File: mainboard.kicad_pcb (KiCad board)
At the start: 2 copper layers, 145.3 x 145.7 mm, 60 parts, among them J1 DRV8833-1, J13 Conn_PCA9685, J14 Conn_01x02, J15 Conn_01x02, J16 Conn_01x02, J18 Screw_Terminal_01x06, J19 Screw_Terminal_01x06, J2 DRV8833-0, J20 Screw_Terminal_01x06, J21 Screw_Terminal_01x06, J22 Screw_Terminal_01x06, J23 Screw_Terminal_01x06, J24 Screw_Terminal_01x04, J25 Screw_Terminal_01x02, J27 Rotary Encoder Conn, J28 Conn_01x02, J3 Conn_01x02, J4 Screw_Terminal_01x06, J5 Screw_Terminal_01x06, J6 VIM4_HEADER, J7 Screw_Terminal_01x06, J8 Screw_Terminal_01x06, Q3 2N7000, Q4 2N7000, U1 MCP23017_SP

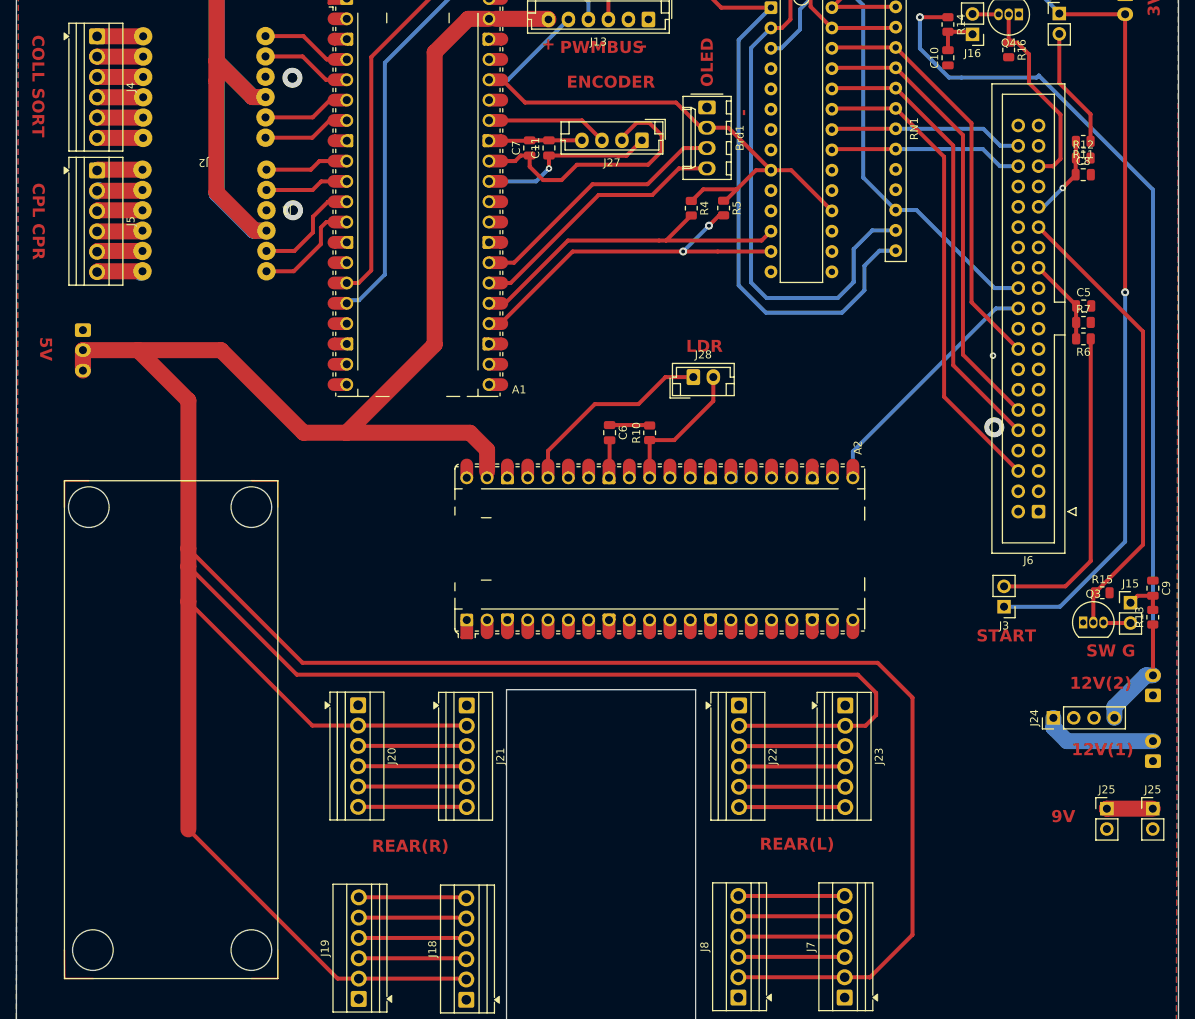
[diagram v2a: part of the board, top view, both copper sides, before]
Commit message: 0 Error DRC mainboard V1.1
Little edits
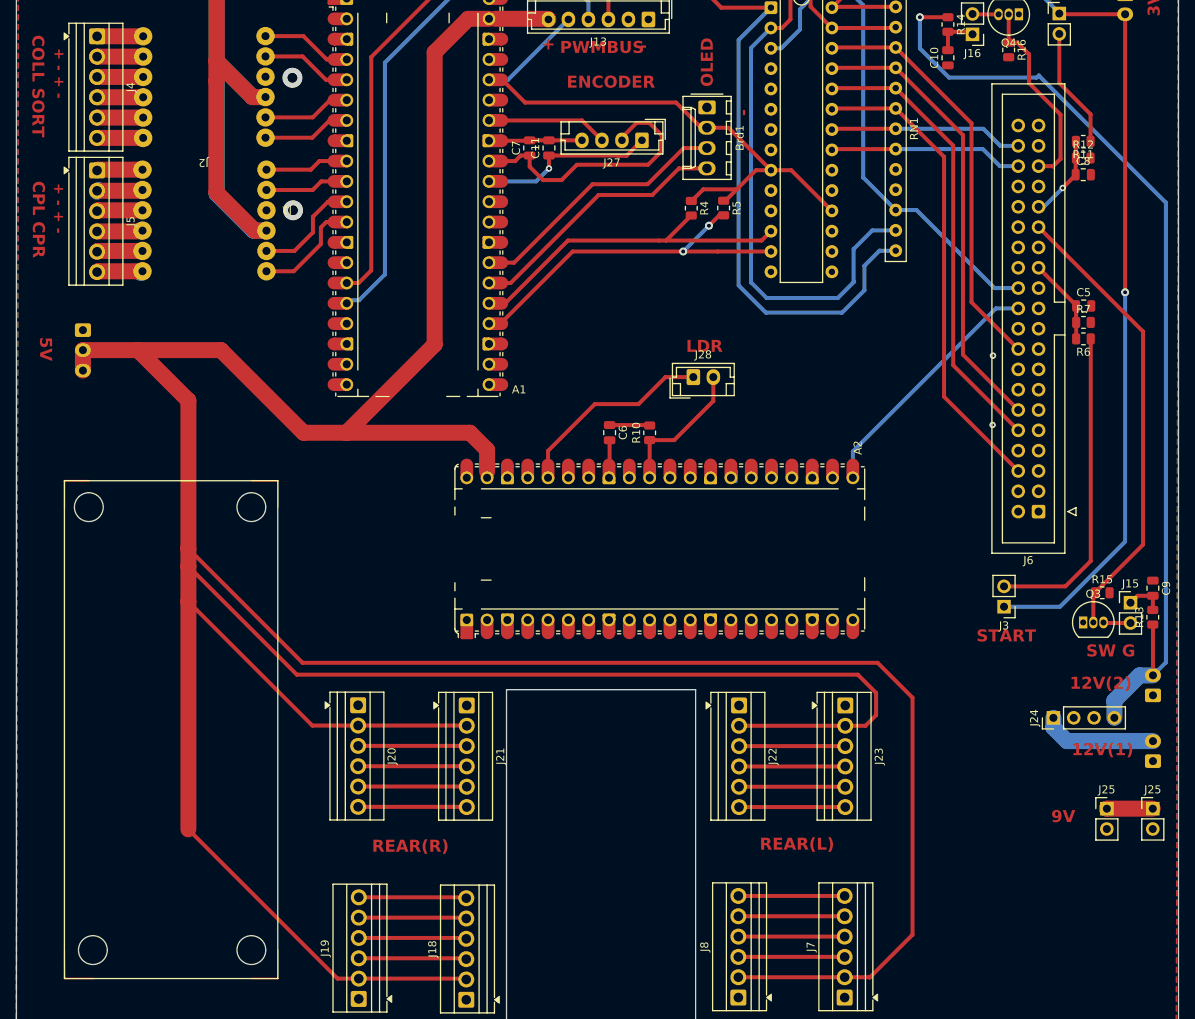
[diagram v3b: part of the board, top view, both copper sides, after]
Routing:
- net 12V_BUCK2: track 119.0 -> 120.8 mm
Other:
- outline, holes or cut-outs redrawn
- board text added: "+ - + -"
- board text removed: "PCA9685"
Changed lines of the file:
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@@
 			(pinfunction "Pin_2")
 			(pintype "passive")
+			(zone_connect 1)
 		)
 		(pad "3" thru_hole circle
@@
 	(gr_circle
 		(center 46.5578 146.5546)
-		(end 48.0818 148.5866)
+		(end 48.3578 146.5546)
 		(stroke
 			(width 0.1)
@@
 	(gr_circle
 		(center 46.5578 91.1826)
-		(end 48.5898 92.7066)
+		(end 48.3578 91.1826)
 		(stroke
 			(width 0.1)
@@
 	(gr_circle
 		(center 26.2378 91.1826)
-		(end 27.7618 93.2146)
+		(end 28.0378 91.1826)
 		(stroke
 			(width 0.1)
@@
 	(gr_circle
 		(center 26.7458 146.5546)
-		(end 28.7778 148.0786)
+		(end 28.5458 146.5546)
 		(stroke
 			(width 0.1)
@@
 		)
 	)
+	(gr_text "+ - + -"
+		(at 21.783395 33.791805 270)
+		(layer "F.Cu")
+		(effects
+			(font
+				(size 1.3 1.3)
+				(thickness 0.3)
+				(bold yes)
+			)
+			(justify left bottom)
+		)
+	)
 	(gr_text "ER0"
 		(at 95.4786 22.6568 90)
@@
 		)
 	)
+	(gr_text "+ - + -"
+		(at 21.732595 50.657405 270)
+		(layer "F.Cu")
+		(effects
+			(font
+				(size 1.3 1.3)
+				(thickness 0.3)
+				(bold yes)
+			)
+			(justify left bottom)
+		)
+	)
 	(gr_text "SW R"
 		(at 133.6798 26.2856 0)
@@
 	)
 	(gr_text "CPL CPR"
-		(at 19.0496 50.6442 270)
+		(at 19.065595 50.403405 270)
 		(layer "F.Cu")
 		(effects
@@
 		)
 	)
-	(gr_text "PCA9685"
-		(at 43.1796 97.6342 270)
+	(gr_text "PWMBUS"
+		(at 25.542595 109.306005 270)
 		(layer "Dwgs.User")
 		(effects
@@
 	)
 	(via
-		(at 139.4206 81.2038)
-		(size 2.5)
-		(drill 1.25)
+		(at 139.207595 80.908805)
+		(size 0.8)
+		(drill 0.4)
 		(layers "F.Cu" "B.Cu")
 		(free yes)
@@
 	)
 	(segment
+		(start 159.2322 128.8762)
+		(end 153.4956 128.8762)
+		(width 2)
+		(layer "F.Cu")
+		(net 29)
+	)
+	(segment
 		(start 153.4956 128.8762)
 		(end 153.4922 128.8796)
@@
 	)
 	(segment
-		(start 159.2322 128.8762)
-		(end 153.4956 128.8762)
+		(start 153.4956 128.8762)
+		(end 153.4922 128.8796)
 		(width 2)
-		(layer "F.Cu")
+		(layer "B.Cu")
 		(net 29)
 	)
@@
 	)
 	(segment
-		(start 133.756 37.487)
-		(end 130.1238 33.8548)
-		(width 0.5)
+		(start 157.585 112.2138)
+		(end 159.2576 112.2138)
+		(width 2)
 		(layer "B.Cu")
 		(net 100)
 	)
 	(segment
-		(start 159.2576 112.2138)
-		(end 159.2576 51.5078)
+		(start 160.873795 53.123995)
+		(end 144.9828 37.233)
 		(width 0.5)
 		(layer "B.Cu")
@@
 	)
 	(segment
-		(start 154.4316 117.5224)
-		(end 154.4316 116.166204)
-		(width 2)
+		(start 160.873795 110.597605)
+		(end 160.873795 53.123995)
+		(width 0.5)
 		(layer "B.Cu")
 		(net 100)
 	)
 	(segment
-		(start 159.2576 51.5078)
-		(end 144.9828 37.233)
+		(start 130.1238 33.8548)
+		(end 130.1238 29.9432)
 		(width 0.5)
 		(layer "B.Cu")
@@
 	)
 	(segment
-		(start 154.4316 116.166204)
-		(end 158.384004 112.2138)
-		(width 2)
+		(start 144.7288 37.487)
+		(end 133.756 37.487)
+		(width 0.5)
 		(layer "B.Cu")
 		(net 100)
 	)
 	(segment
-		(start 135.3054 37.487)
-		(end 133.756 37.487)
+		(start 133.756 37.487)
+		(end 130.1238 33.8548)
 		(width 0.5)
 		(layer "B.Cu")
@@
 	)
 	(segment
-		(start 144.9828 37.233)
-		(end 144.7288 37.487)
+		(start 159.2576 112.2138)
+		(end 160.873795 110.597605)
 		(width 0.5)
 		(layer "B.Cu")
@@
 	)
 	(segment
-		(start 158.384004 112.2138)
-		(end 159.2576 112.2138)
+		(start 154.4316 117.5224)
+		(end 154.4316 115.3672)
 		(width 2)
 		(layer "B.Cu")
@@
 	)
 	(segment
-		(start 130.1238 33.8548)
-		(end 130.1238 29.9432)
+		(start 144.9828 37.233)
+		(end 144.7288 37.487)
 		(width 0.5)
 		(layer "B.Cu")
@@
 	)
 	(segment
-		(start 144.7288 37.487)
-		(end 135.3054 37.487)
-		(width 0.5)
+		(start 154.4316 115.3672)
+		(end 157.585 112.2138)
+		(width 2)
 		(layer "B.Cu")
 		(net 100)
@@
 		)
 	)
-	(group ""
-		(members "10e107f0-c7ad-4d40-99a2-7dc670773874" "12d0a75c-97f8-44c2-a897-3730a86650cc"
-			"27245aee-9862-402e-b8c8-fd2e73fa7211" "2b991e7c-9771-4b05-9140-cff9aca4e192"
-			"32c44921-4a61-4ea6-affd-730ccbc1ac79" "371a8fa8-4237-460a-9dff-3feb19b7b641"
-			"5ec19375-977e-460d-8900-7bd6bb5fc823" "5eddb3c7-0444-4fad-acf5-7022e4e61d0d"
-			"62c0df71-baf8-43e1-8f33-aed2d82cffd4" "63ef0ea2-1e38-4669-a243-0d48b2a4169b"
-			"6935ae09-6457-4e95-b84d-12b1252e048c" "80397a6b-8b9f-4cee-8c91-364920eb0ab2"
-			"8faa41af-d048-4e7e-9dcd-a359f8712989" "a868eac6-c5ab-4666-ac2a-ef669558a232"
-			"ac566b10-f30f-44ca-9430-312e8e88fd2f" "b06870c7-e6db-4085-b265-dfabf63b7a0f"
-			"b669a6bb-dac8-4b01-9778-a2f7c12d4540" "bf67e102-4a23-454e-b20e-9be1b0ded58d"
-			"d23251ce-8760-4af8-9f6b-6149fd86dd9a" "dde7e079-292d-4eda-9f78-bd0779382894"
-			"f003b019-fce3-4eef-8b46-9bc71a189fcb" "f2f67e28-22a0-4ece-b64c-0ce0855e54dc"
-			"f332a343-dcfe-4f90-a448-aa52f8ab617e"
-		)
-	)

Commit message: 0 Error DRC mainboard V1.15
Placed motor interface within boundaries, rounded off edge.cuts with some arcs.

resized all of the pads to 2mm

got rid of some islands and their associated vias.

***This version has the chassis DXF in the PCB editor.
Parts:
- moved C6 252.9 mm to (344.2, 86.4)
- moved A2 252.9 mm to (350.5, 100.9)
- moved R10 252.9 mm to (349.2, 86.4)
- moved ? 245.6 mm to (400.8, 45.9)
- moved ? 245.6 mm to (400.8, 43.4)
- moved A1 245.6 mm to (312.4, 68.0)
- moved Brd1 245.6 mm to (348.5, 57.5)
- moved C5 245.6 mm to (395.6, 82.3)
- moved C8 245.6 mm to (395.6, 65.9)
- moved J14 245.6 mm to (392.6, 45.8)
- moved J15 245.6 mm to (401.5, 119.4)
- moved J16 245.6 mm to (381.7, 48.4)
- moved J2 245.6 mm to (295.0, 47.0)
- moved J24 245.6 mm to (391.8, 133.8)
- moved J27 245.6 mm to (340.4, 61.6)
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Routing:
- net 5V_BUCK: track 539.6 -> 390.1 mm
- net PIC_STATE: track 31.4 -> 16.7 mm
- net PICO2_3V3: track 24.5 -> 15.3 mm
- net LDR_ADC: track 16.9 -> 13.7 mm
- net unconnected-(A2-GPIO21-Pad27)_1 (its old number): track 1.31 -> 0.00 mm
- net GND: track 0.10 -> 0.41 mm, vias 4 -> 2
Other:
- board size 145.3 x 145.7 mm -> 157.6 x 135.8 mm

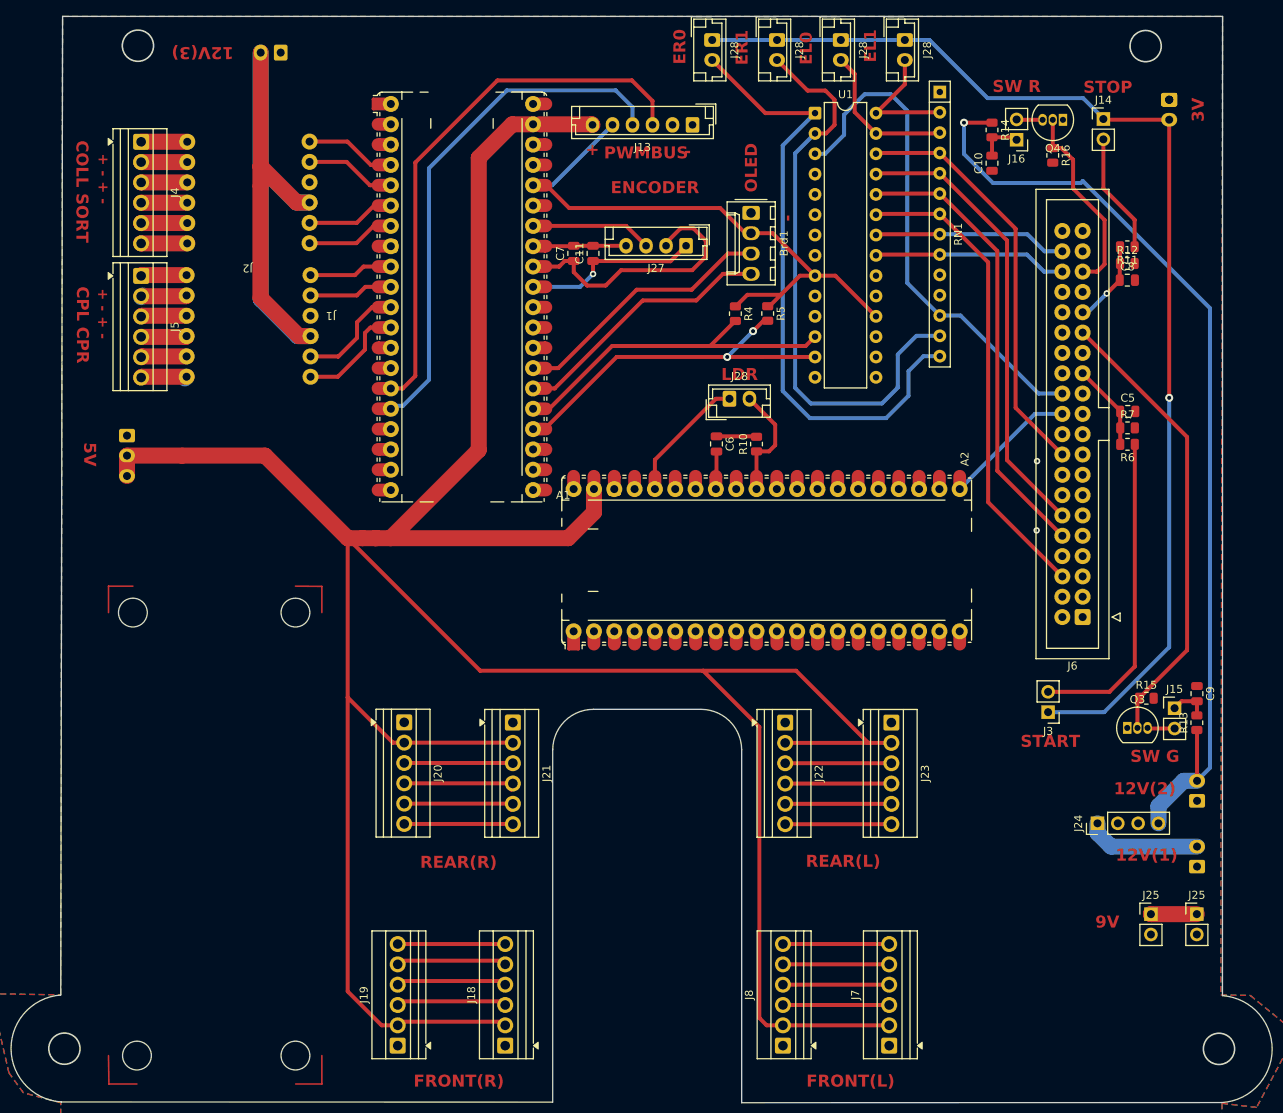
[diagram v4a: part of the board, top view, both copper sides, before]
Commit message: Validated mainboard V1.15
0 Error 0 Warnings

Ready for Ochoa chack
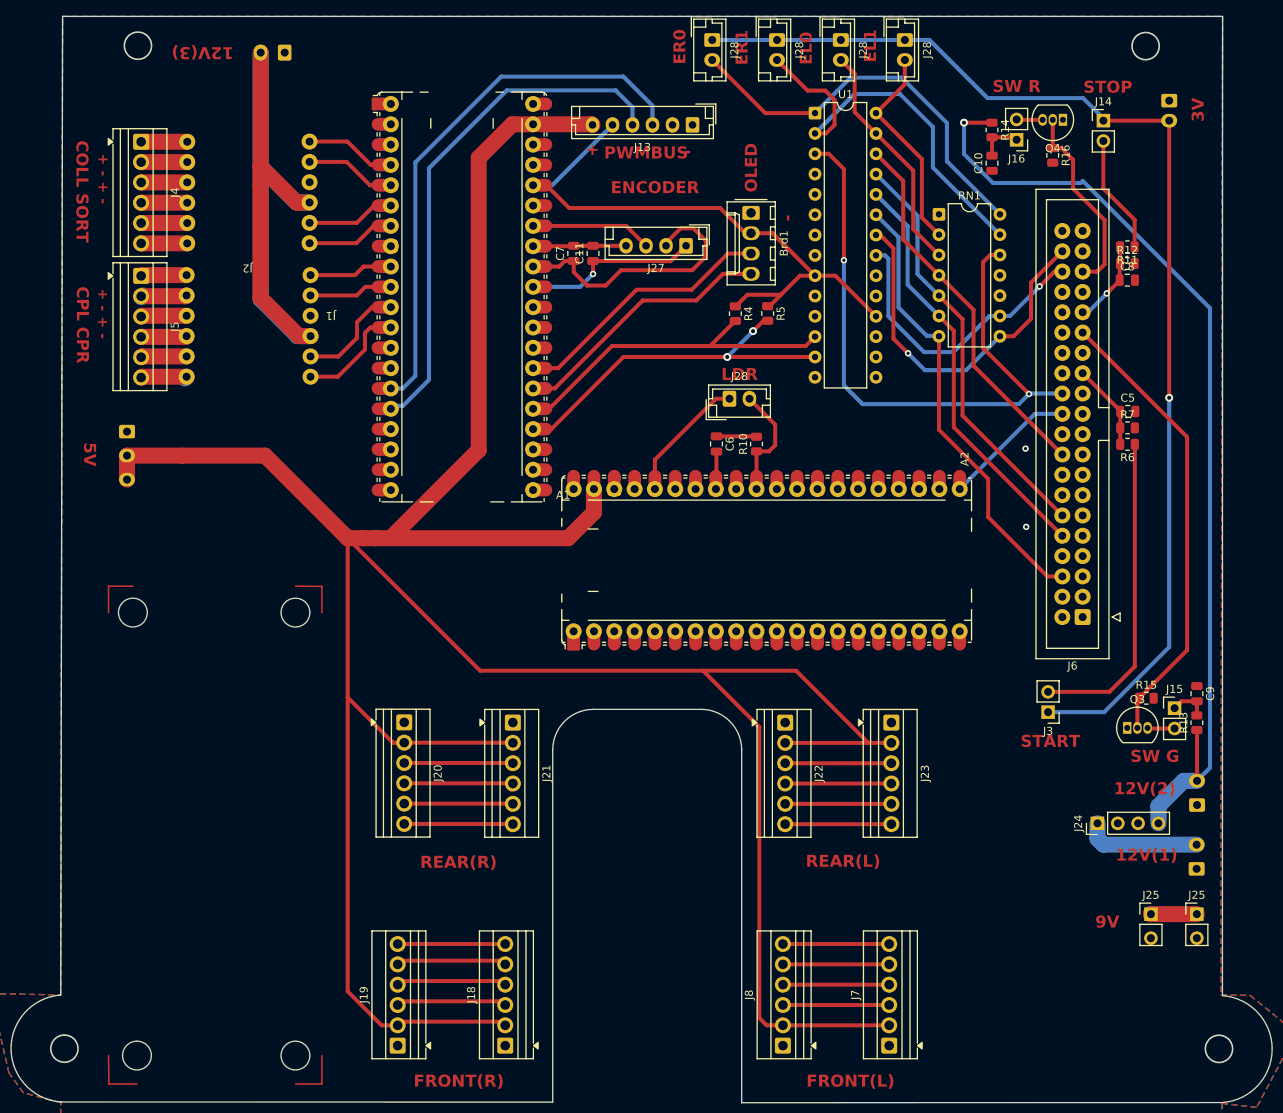
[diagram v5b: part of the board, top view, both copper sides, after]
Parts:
- removed the ? at (404.3, 139.2)
- removed the ? at (404.3, 136.7)
- removed the ? at (270.5, 90.4)
- removed the ? at (400.8, 43.4)
- added ?: , clipboard:9e3165f1-3c62-4009-ad41-a695cb7dbfe7, F.Cu at (404.2, 136.5)
- RN1: footprint Resistor_THT:R_Array_SIP14 -> Package_DIP:DIP-14_W7.62mm
- moved RN1 15.3 mm to (372.0, 57.7), turned to 0 degrees
- moved J14 0.21 mm to (392.6, 46.0)
- moved ? 0.12 mm to (400.8, 46.0)
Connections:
- A2 pad 10: (no net) -> unconnected-(A2-GPIO7-Pad10)_1
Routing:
- net CP-R-ENDSTOP0: track 78.1 -> 50.4 mm
- net CP-R-ENDSTOP1: track 73.0 -> 50.7 mm
- net SORT(en/dis): track 24.2 -> 45.9 mm, vias 0 -> 1
- net TOTEM-EXTEND: track 63.6 -> 81.6 mm, vias 0 -> 2
- net COLL(en/dis): track 24.2 -> 36.8 mm, vias 0 -> 1
- net CP-L-ENDSTOP1: track 16.2 -> 26.7 mm
- net CP-L-ENDSTOP0: track 19.0 -> 29.5 mm
- net DOOR-R: track 52.1 -> 47.4 mm
- net DOOR-L: track 57.1 -> 52.5 mm
- net CP-R: track 57.1 -> 52.5 mm
- net CP-L: track 59.7 -> 57.0 mm
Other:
- outline, holes or cut-outs redrawn
